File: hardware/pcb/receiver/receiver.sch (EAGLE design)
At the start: 42 parts, among them IC3 LM1117-5.0, IC4 TPS73733, X1 SMA

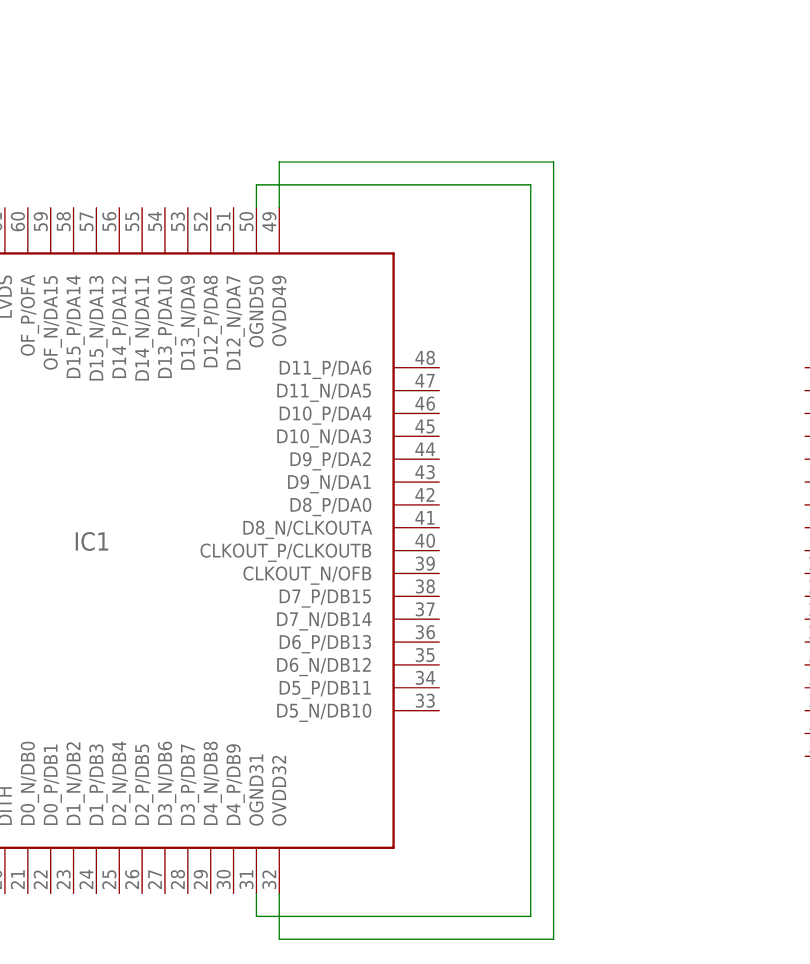
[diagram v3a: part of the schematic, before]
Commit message: hw: added bibliography and hpsdr schematic hw: modified reciever - power supply
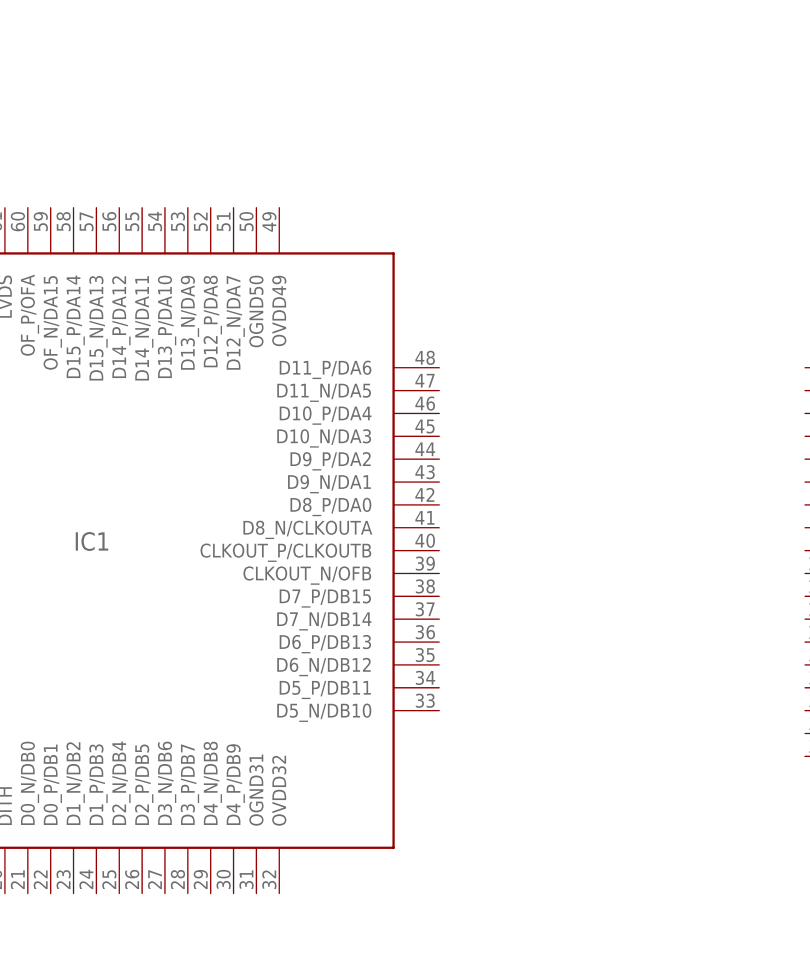
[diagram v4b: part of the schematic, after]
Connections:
- removed net N$10: IC1.OVDD32, IC1.OVDD49
- removed net N$6: IC1.OGND31, IC1.OGND50
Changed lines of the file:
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@@
 <setting verticaltext="up"/>
 </settings>
-<grid distance="0.1" unitdist="inch" unit="inch" style="lines" multiple="1" display="yes" altdistance="0.05" altunitdist="inch" altunit="inch"/>
+<grid distance="0.1" unitdist="inch" unit="inch" style="lines" multiple="1" display="yes" altdistance="0.01" altunitdist="inch" altunit="inch"/>
 <layers>
 <layer number="1" name="Top" color="4" fill="1" visible="no" active="no"/>
@@
 <part name="P+2" library="supply1" deviceset="+5V" device=""/>
 <part name="P+3" library="supply1" deviceset="+5V" device=""/>
-<part name="SV1" library="lstolcman_thesis" deviceset="PINHEADER" device=""/>
 <part name="IC2" library="lstolcman_thesis" deviceset="LTC6405" device=""/>
 <part name="C2" library="rcl" deviceset="C-EU" device="C0805" value="2,2u"/>
@@
 <part name="GND17" library="supply1" deviceset="GND" device=""/>
 <part name="GND18" library="supply1" deviceset="GND" device=""/>
+<part name="SV1" library="lstolcman_thesis" deviceset="PINHEADER" device=""/>
 </parts>
 <sheets>
@@
 <instance part="P+2" gate="1" x="78.74" y="63.5"/>
 <instance part="P+3" gate="1" x="121.92" y="99.06"/>
-<instance part="SV1" gate="G$1" x="294.64" y="33.02"/>
 <instance part="IC2" gate="G$1" x="81.28" y="40.64"/>
 <instance part="C2" gate="G$1" x="121.92" y="91.44"/>
@@
 <instance part="GND17" gate="1" x="83.82" y="99.06"/>
 <instance part="GND18" gate="1" x="50.8" y="99.06"/>
+<instance part="SV1" gate="G$1" x="294.64" y="33.02"/>
 </instances>
 <busses>
@@
 </segment>
 <segment>
-<pinref part="SV1" gate="G$1" pin="GND"/>
 <wire x1="297.18" y1="7.62" x2="297.18" y2="5.08" width="0.1524" layer="91"/>
 <label x="297.18" y="5.08" size="1.27" layer="95" rot="R270" xref="yes"/>
+<pinref part="SV1" gate="G$1" pin="GND"/>
 </segment>
 <segment>
@@
 </segment>
 </net>
-<net name="N$6" class="0">
-<segment>
-<pinref part="IC1" gate="G$1" pin="OGND31"/>
-<wire x1="210.82" y1="0" x2="210.82" y2="-2.54" width="0.1524" layer="91"/>
-<wire x1="210.82" y1="-2.54" x2="241.3" y2="-2.54" width="0.1524" layer="91"/>
-<wire x1="241.3" y1="-2.54" x2="241.3" y2="78.74" width="0.1524" layer="91"/>
-<pinref part="IC1" gate="G$1" pin="OGND50"/>
-<wire x1="241.3" y1="78.74" x2="210.82" y2="78.74" width="0.1524" layer="91"/>
-<wire x1="210.82" y1="78.74" x2="210.82" y2="76.2" width="0.1524" layer="91"/>
-</segment>
-</net>
-<net name="N$10" class="0">
-<segment>
-<pinref part="IC1" gate="G$1" pin="OVDD49"/>
-<wire x1="213.36" y1="76.2" x2="213.36" y2="81.28" width="0.1524" layer="91"/>
-<wire x1="213.36" y1="81.28" x2="243.84" y2="81.28" width="0.1524" layer="91"/>
-<wire x1="243.84" y1="81.28" x2="243.84" y2="-5.08" width="0.1524" layer="91"/>
-<pinref part="IC1" gate="G$1" pin="OVDD32"/>
-<wire x1="243.84" y1="-5.08" x2="213.36" y2="-5.08" width="0.1524" layer="91"/>
-<wire x1="213.36" y1="-5.08" x2="213.36" y2="0" width="0.1524" layer="91"/>
-</segment>
-</net>

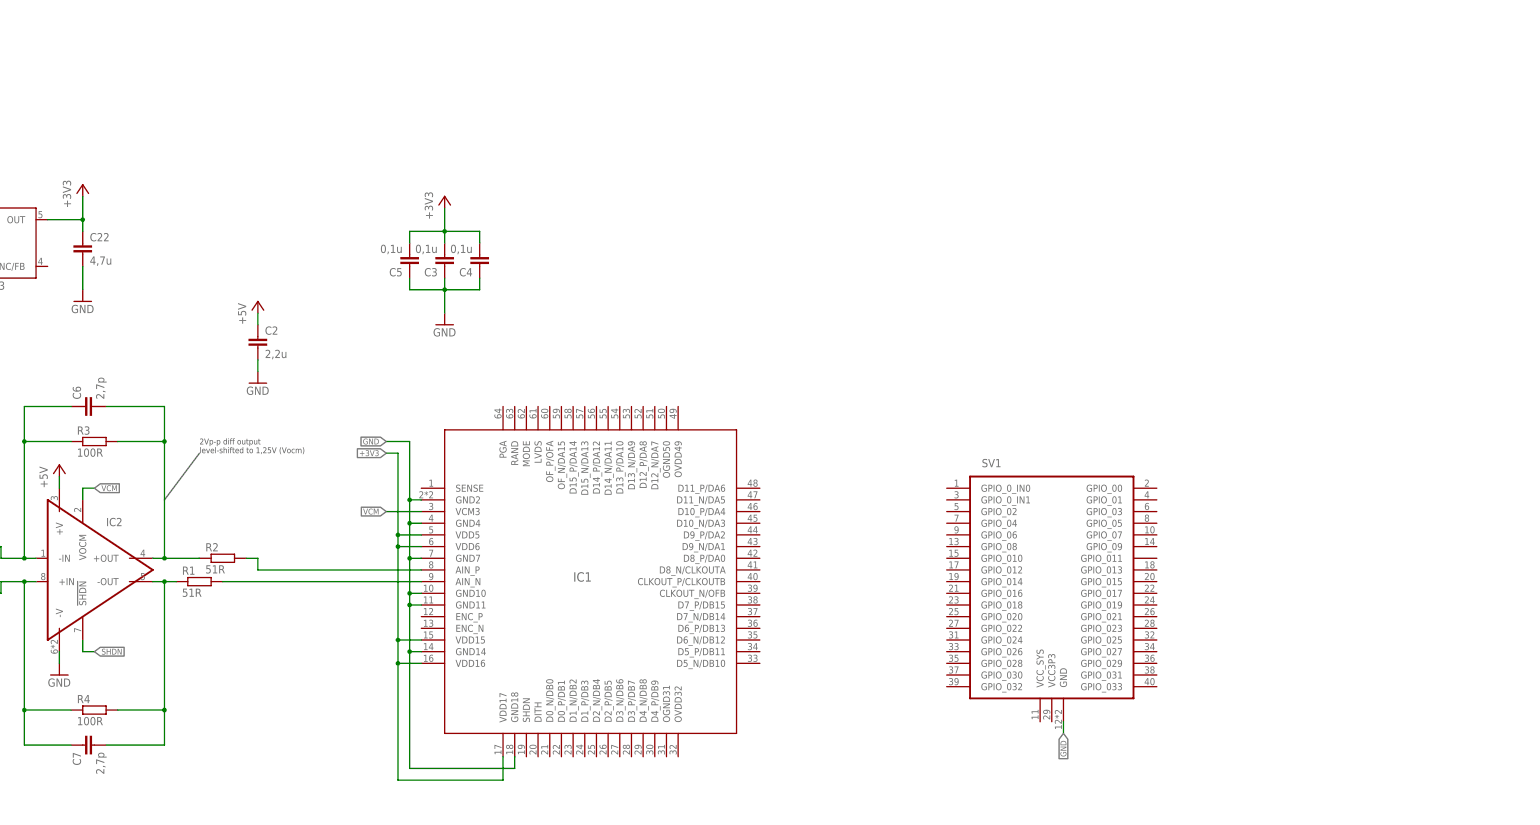
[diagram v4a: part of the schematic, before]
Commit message: hw: added filtering to adc hw: added mode switch to adc
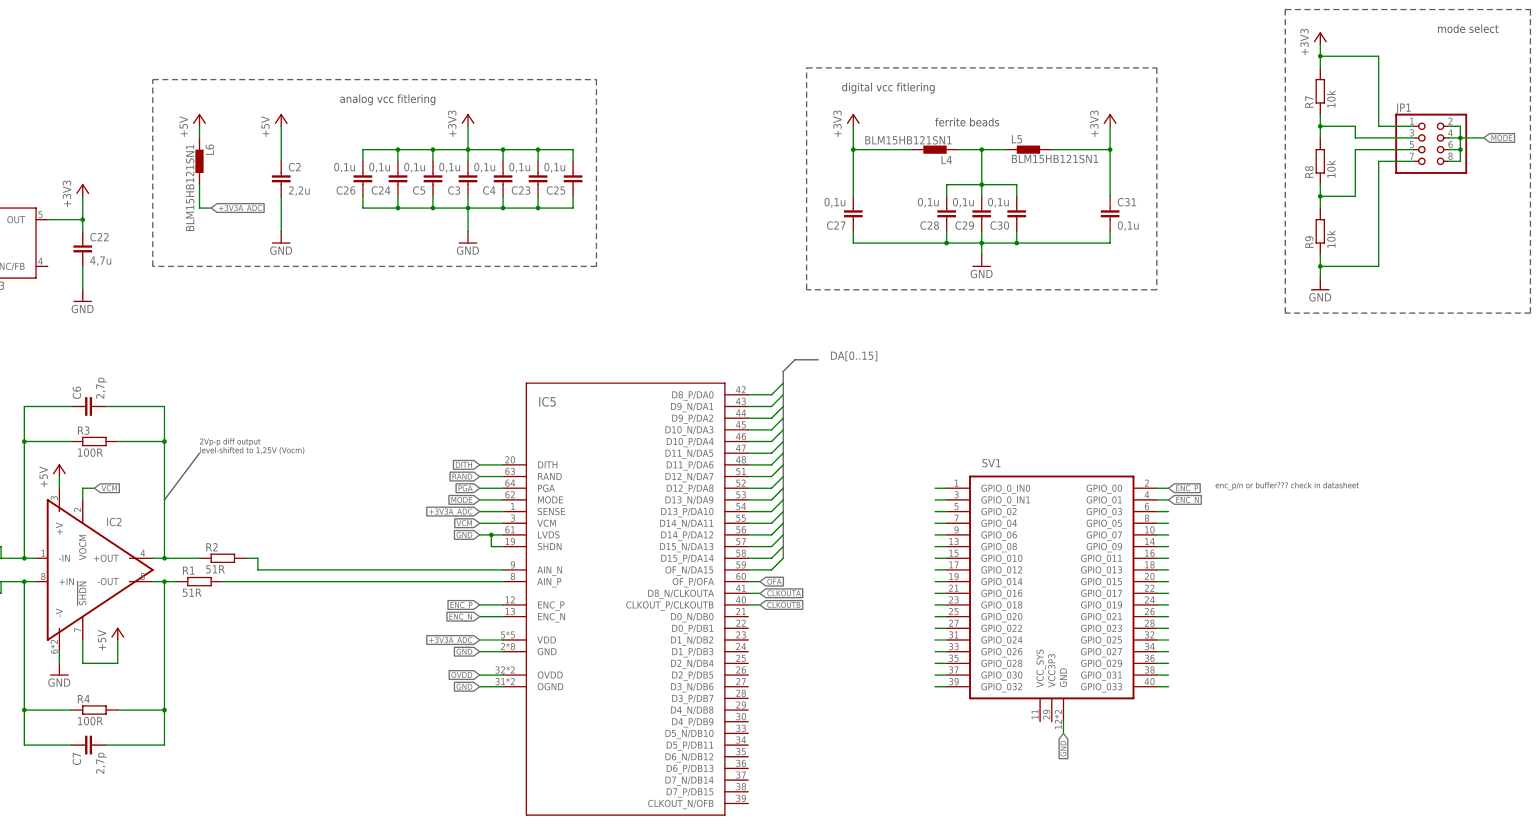
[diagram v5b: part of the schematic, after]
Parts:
- removed IC1: (no value), lstolcman_thesis:LTC2208_BOX
- added C23, C24, C25, C26, C27, C28, C29, C30, C31: 0,1u, rcl:C-EUC0805
- added IC5: (no value), lstolcman_thesis:LTC2208_FLAT
- added JP1: (no value), pinhead:PINHD-2X4
- added L4, L5, L6: BLM15HB121SN1, inductors:BLM15HB121SN1
- added R7, R8, R9: 10k, rcl:R-EU_M1206
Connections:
- removed net SHDN: IC2.!SHDN
- new net +3V3A_ADC: IC5.SENSE, IC5.VDD, L6.2
- new net CLKOUTA: IC5.D8_N/CLKOUTA
- new net CLKOUTB: IC5.CLKOUT_P/CLKOUTB
- new net DA0: IC5.D8_P/DA0
- new net DA1: IC5.D9_N/DA1
- new net DA10: IC5.D13_P/DA10
- new net DA11: IC5.D14_N/DA11
- new net DA12: IC5.D14_P/DA12
- new net DA13: IC5.D15_N/DA13
- new net DA14: IC5.D15_P/DA14
- new net DA15: IC5.OF_N/DA15
- new net DA2: IC5.D9_P/DA2
- new net DA3: IC5.D10_N/DA3
- new net DA4: IC5.D10_P/DA4
- new net DA5: IC5.D11_N/DA5
- new net DA6: IC5.D11_P/DA6
- new net DA7: IC5.D12_N/DA7
- new net DA8: IC5.D12_P/DA8
- new net DA9: IC5.D13_N/DA9
- new net DITH: IC5.DITH
- new net ENC_N: IC5.ENC_N, SV1.GPIO_01
- new net ENC_P: IC5.ENC_P, SV1.GPIO_00
- new net IN_N: IC5.AIN_P, R1.2
- new net IN_P: IC5.AIN_N, R2.2
- new net MODE: IC5.MODE, JP1.2, JP1.4, JP1.6, JP1.8
- new net N$10: SV1.GPIO_03
- new net N$20: SV1.GPIO_07
- new net N$21: SV1.GPIO_09
- new net N$22: SV1.GPIO_011
- new net N$23: SV1.GPIO_013
- new net N$24: SV1.GPIO_015
- new net N$25: SV1.GPIO_017
- new net N$26: SV1.GPIO_019
- new net N$27: SV1.GPIO_021
- new net N$28: SV1.GPIO_023
- new net N$29: SV1.GPIO_025
- new net N$30: SV1.GPIO_027
- new net N$31: SV1.GPIO_029
- new net N$32: SV1.GPIO_031
- new net N$33: SV1.GPIO_033
- new net N$34: SV1.GPIO_0_IN0
- new net N$35: SV1.GPIO_0_IN1
- new net N$36: SV1.GPIO_02
- new net N$37: SV1.GPIO_04
- new net N$38: SV1.GPIO_06
- new net N$39: SV1.GPIO_08
- new net N$40: SV1.GPIO_010
- new net N$41: SV1.GPIO_012
- new net N$42: SV1.GPIO_014
- new net N$43: SV1.GPIO_016
- new net N$44: SV1.GPIO_018
- new net N$45: SV1.GPIO_020
- new net N$46: SV1.GPIO_022
- new net N$47: SV1.GPIO_024
- new net N$48: SV1.GPIO_026
- new net N$49: SV1.GPIO_028
- new net N$50: SV1.GPIO_030
- new net N$51: SV1.GPIO_032
- new net N$6: JP1.3, R7.1, R8.2
- new net OFA: IC5.OF_P/OFA
- new net OVDD: C28.2, C29.2, C30.2, IC5.OVDD, L4.1, L5.1
- new net PGA: IC5.PGA
- new net RAND: IC5.RAND
- net +3V3: now also C23.2, C24.2, C25.2, C26.2, C27.2, C31.1, JP1.1, L4.2, L5.2, R7.2; no longer IC1.VDD15, IC1.VDD16, IC1.VDD17, IC1.VDD5, IC1.VDD6
- net +5V: now also IC2.!SHDN, L6.1
- net GND: now also C23.1, C24.1, C25.1, C26.1, C27.1, C28.1, C29.1, C30.1, C31.2, IC2.-V, IC5.GND, IC5.LVDS, IC5.OGND, IC5.SHDN, JP1.7, R9.1; no longer IC1.GND10, IC1.GND11, IC1.GND14, IC1.GND18, IC1.GND2, IC1.GND4, IC1.GND7
- net N$11: now also SV1.GPIO_05; no longer IC1.AIN_N, R1.2
- net N$9: now also JP1.5, R8.1, R9.2; no longer IC1.AIN_P, R2.2
- net VCM: now also IC5.VCM; no longer IC1.VCM3
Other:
- note added: "analog vcc fitlering"
- note added: "digital vcc fitlering"
- note added: "enc_p/n or buffer??? check in datasheet"
- note added: "ferrite beads"
- note added: "mode select"
- moved on the sheet: C2, C3, C4, C5

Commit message: hw-receiver: added filter between amp and adc, minor changes
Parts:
- removed L4, L5, L6: BLM15HB121SN1, inductors:BLM15HB121SN1
- added C32: 100n, rcl:C-EUC0805
- added C33: 100p, rcl:C-EUC0805
- added C34: 2,2u, rcl:C-EUC0805
- added L7, L8, L9: ferrite bead, inductor-neosid:SM-NE29
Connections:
- removed net OVDD: C28.2, C29.2, C30.2, IC5.OVDD, L4.1, L5.1
- new net VDD: C28.2, C29.2, C30.2, IC5.OVDD, L8.1, L9.2
- net +3V3: now also L8.2, L9.1; no longer L4.2, L5.2
- net +3V3A_ADC: now also L7.1; no longer L6.2
- net +5V: now also L7.2; no longer L6.1
- net GND: now also C34.1
- net IN_N: now also C33.2
- net IN_P: now also C33.1
- net VCM: now also C34.2
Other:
- note added: "cap between sma and diode?"
- note added: "clkout differential to fpga as clk?"
- note added: "enc is lvpecl!!!!"
- note added: "optional cap for RC/LC filter"
- note added: "use mc100lvelt22!"
- note removed: "2Vp-p diff output level-shifted to 1,25V (Vocm)"
- note removed: "ferrite beads"
- moved on the sheet: R1, R2

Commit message: hw-receiver: created regions of power supply hw: added doc about decoupling
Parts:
- added C35, C36, C37: 100n, rcl:C-EUC0805
- added L4, L5: ferrite bead, inductor-neosid:SM-NE29
- added R10: 1M, rcl:R-EU_M1206
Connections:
- new net +5V_AMP: C37.2, IC2.!SHDN, IC2.+V, L5.1
- new net N$52: C32.1, R10.2, X1.1
- new net N$53: C2.1, L4.1, L5.2
- net +3V3: now also C35.1
- net +5V: now also C36.1, L4.2; no longer C2.1, IC2.!SHDN, IC2.+V
- net GND: now also C35.2, C36.2, C37.1, R10.1
- net N$2: now also C32.2; no longer X1.1
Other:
- note added: "adc analog vcc fitlering"
- note added: "adc digital vcc fitlering"
- note added: "adc mode select"
- note added: "amp filtering"
- note added: "general +3.3v supply"
- note added: "general +5v supply"
- note added: "http://www.electro-labs.com/bypass-capacitors-why-and-how-to-use-them/"
- note added: "ptc?"
- note removed: "analog vcc fitlering"
- note removed: "cap between sma and diode?"
- note removed: "digital vcc fitlering"
- note removed: "mode select"
- moved on the sheet: C1, C17, C18, C19, C2, C20, C21, C22, C23, C24, C25, C26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

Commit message: hw: added lvttl to lvpecl enc inputs translator
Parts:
- added V1: SY100EPT22, lstolcman_thesis:SY100EPT22
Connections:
- removed net ENC_N: IC5.ENC_N, SV1.GPIO_01
- removed net ENC_P: IC5.ENC_P, SV1.GPIO_00
- removed net N$11 (its old number): SV1.GPIO_05
- removed net N$26 (its old number): SV1.GPIO_019
- removed net N$27: SV1.GPIO_021
- removed net N$28: SV1.GPIO_023
- removed net N$29 (its old number): SV1.GPIO_025
- removed net N$30 (its old number): SV1.GPIO_027
- removed net N$31 (its old number): SV1.GPIO_029
- removed net N$32 (its old number): SV1.GPIO_031
- removed net N$33 (its old number): SV1.GPIO_033
- removed net N$40: SV1.GPIO_010
- removed net N$41: SV1.GPIO_012
- removed net N$42: SV1.GPIO_014
- removed net N$43: SV1.GPIO_016
- removed net N$44: SV1.GPIO_018
- removed net N$45: SV1.GPIO_020
- removed net N$46: SV1.GPIO_022
- removed net N$47: SV1.GPIO_024
- removed net N$48: SV1.GPIO_026
- removed net N$49: SV1.GPIO_028
- removed net N$50: SV1.GPIO_030
- removed net N$51: SV1.GPIO_032
- new net ENC: SV1.GPIO_05, V1.D0
- new net N$20: IC5.ENC_P, V1.Q0
- new net N$23: IC5.ENC_N, V1.!Q0
- net +3V3: now also V1.VCC
- net CLKOUTA: now also SV1.GPIO_0_IN0
- net CLKOUTB: now also SV1.GPIO_0_IN1
- net DA0: now also SV1.GPIO_019
- net DA1: now also SV1.GPIO_021
- net DA10: now also SV1.GPIO_028
- net DA11: now also SV1.GPIO_026
- net DA12: now also SV1.GPIO_024
- net DA13: now also SV1.GPIO_022
- net DA14: now also SV1.GPIO_020
- net DA15: now also SV1.GPIO_018
- net DA2: now also SV1.GPIO_023
- net DA3: now also SV1.GPIO_025
- net DA4: now also SV1.GPIO_027
- net DA5: now also SV1.GPIO_029
- net DA6: now also SV1.GPIO_031
- net DA7: now also SV1.GPIO_033
- net DA8: now also SV1.GPIO_032
- net DA9: now also SV1.GPIO_030
- net GND: now also V1.GND
- net N$34: now also SV1.GPIO_01; no longer SV1.GPIO_0_IN0
- net N$35: now also SV1.GPIO_00; no longer SV1.GPIO_0_IN1
- net OFA: now also SV1.GPIO_016
- net PGA: now also SV1.GPIO_010
- net RAND: now also SV1.GPIO_012
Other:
- note added: "http://electronics.stackexchange.com/questions/15135/decoupling-caps-pcb-layout"
- note added: "or mc100lvelt22!"
- note removed: "clkout differential to fpga as clk?"
- note removed: "enc_p/n or buffer??? check in datasheet"
- note removed: "use mc100lvelt22!"
